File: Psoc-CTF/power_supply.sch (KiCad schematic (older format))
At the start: 12 parts

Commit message: Generación de lista de materiales
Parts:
- gave numbers to parts that had none: 12
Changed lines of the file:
@@
 $EndDescr
 $Comp
-L Regulator_Linear:AMS1117-5.0 U?
+L Regulator_Linear:AMS1117-5.0 U2
 U 1 1 621012EE
 P 2050 1700
-F 0 "U?" H 2050 1942 50  0000 C CNN
+F 0 "U2" H 2050 1942 50  0000 C CNN
 F 1 "AMS1117-5.0" H 2050 1851 50  0000 C CNN
 F 2 "Package_TO_SOT_SMD:SOT-223-3_TabPin2" H 2050 1900 50  0001 C CNN
@@
 $EndComp
 $Comp
-L Device:C C?
+L Device:C C5
 U 1 1 621012F4
 P 2950 1850
-F 0 "C?" H 3065 1896 50  0000 L CNN
+F 0 "C5" H 3065 1896 50  0000 L CNN
 F 1 "10uF" H 3065 1805 50  0000 L CNN
 F 2 "Capacitor_SMD:C_0603_1608Metric_Pad1.08x0.95mm_HandSolder" H 2988 1700 50  0001 C CNN
@@
 $EndComp
 $Comp
-L Device:CP C?
+L Device:CP C1
 U 1 1 621012FA
 P 1450 1850
-F 0 "C?" H 1568 1896 50  0000 L CNN
+F 0 "C1" H 1568 1896 50  0000 L CNN
 F 1 "100uF" H 1568 1805 50  0000 L CNN
 F 2 "Capacitor_SMD:C_0805_2012Metric_Pad1.18x1.45mm_HandSolder" H 1488 1700 50  0001 C CNN
@@
 $EndComp
 $Comp
-L Device:CP C?
+L Device:CP C3
 U 1 1 62101300
 P 2500 1850
-F 0 "C?" H 2618 1896 50  0000 L CNN
+F 0 "C3" H 2618 1896 50  0000 L CNN
 F 1 "10uF" H 2618 1805 50  0000 L CNN
 F 2 "Capacitor_SMD:C_0805_2012Metric_Pad1.18x1.45mm_HandSolder" H 2538 1700 50  0001 C CNN
@@
 Vin
 $Comp
-L power:GND #PWR?
+L power:GND #PWR05
 U 1 1 62101312
 P 2050 2000
-F 0 "#PWR?" H 2050 1750 50  0001 C CNN
+F 0 "#PWR05" H 2050 1750 50  0001 C CNN
 F 1 "GND" H 2055 1827 50  0000 C CNN
 F 2 "" H 2050 2000 50  0001 C CNN
@@
 Connection ~ 1800 3375
 $Comp
-L power:GND #PWR?
+L power:GND #PWR04
 U 1 1 62101319
 P 1800 3375
-F 0 "#PWR?" H 1800 3125 50  0001 C CNN
+F 0 "#PWR04" H 1800 3125 50  0001 C CNN
 F 1 "GND" H 1805 3202 50  0000 C CNN
 F 2 "" H 1800 3375 50  0001 C CNN
@@
 	2100 3075 2300 3075
 $Comp
-L Device:C C?
+L Device:C C4
 U 1 1 62101325
 P 2750 3225
-F 0 "C?" H 2865 3271 50  0000 L CNN
+F 0 "C4" H 2865 3271 50  0000 L CNN
 F 1 "10uF" H 2865 3180 50  0000 L CNN
 F 2 "Capacitor_SMD:C_0603_1608Metric_Pad1.08x0.95mm_HandSolder" H 2788 3075 50  0001 C CNN
@@
 $EndComp
 $Comp
-L Device:CP C?
+L Device:CP C2
 U 1 1 6210132B
 P 2300 3225
-F 0 "C?" H 2418 3271 50  0000 L CNN
+F 0 "C2" H 2418 3271 50  0000 L CNN
 F 1 "10uF" H 2418 3180 50  0000 L CNN
 F 2 "Capacitor_SMD:C_0805_2012Metric_Pad1.18x1.45mm_HandSolder" H 2338 3075 50  0001 C CNN
@@
 	1250 3075 1500 3075
 $Comp
-L Regulator_Linear:AMS1117-3.3 U?
+L Regulator_Linear:AMS1117-3.3 U1
 U 1 1 62101332
 P 1800 3075
-F 0 "U?" H 1800 3317 50  0000 C CNN
+F 0 "U1" H 1800 3317 50  0000 C CNN
 F 1 "AMS1117-3.3" H 1800 3226 50  0000 C CNN
 F 2 "Package_TO_SOT_SMD:SOT-223-3_TabPin2" H 1800 3275 50  0001 C CNN
@@
 3.3V POWER SUPPLY
 $Comp
-L power:+3.3V #PWR?
+L power:+3.3V #PWR09
 U 1 1 6210133B
 P 2750 3075
-F 0 "#PWR?" H 2750 2925 50  0001 C CNN
+F 0 "#PWR09" H 2750 2925 50  0001 C CNN
 F 1 "+3.3V" H 2765 3248 50  0000 C CNN
 F 2 "" H 2750 3075 50  0001 C CNN
@@
 Connection ~ 2750 3075
 $Comp
-L power:+5V #PWR?
+L power:+5V #PWR02
 U 1 1 62101342
 P 1250 3075
-F 0 "#PWR?" H 1250 2925 50  0001 C CNN
+F 0 "#PWR02" H 1250 2925 50  0001 C CNN
 F 1 "+5V" H 1250 3250 50  0000 C CNN
 F 2 "" H 1250 3075 50  0001 C CNN
@@
 P 1600 4050
 AR Path="/621106AB" Ref="#PWR?"  Part="1"
-AR Path="/620E3406/621106AB" Ref="#PWR?"  Part="1"
-F 0 "#PWR?" H 1600 3900 50  0001 C CNN
+AR Path="/620E3406/621106AB" Ref="#PWR03"  Part="1"
+F 0 "#PWR03" H 1600 3900 50  0001 C CNN
 F 1 "VDD" V 1600 4175 50  0000 L CNN
 F 2 "" H 1600 4050 50  0001 C CNN
@@
 P 1100 4050
 AR Path="/621106B4" Ref="#PWR?"  Part="1"
-AR Path="/620E3406/621106B4" Ref="#PWR?"  Part="1"
-F 0 "#PWR?" H 1100 3900 50  0001 C CNN
+AR Path="/620E3406/621106B4" Ref="#PWR01"  Part="1"
+F 0 "#PWR01" H 1100 3900 50  0001 C CNN
 F 1 "+3.3V" V 1100 4325 50  0000 C CNN
 F 2 "" H 1100 4050 50  0001 C CNN
@@
 P 2500 4225
 AR Path="/621106C5" Ref="#PWR?"  Part="1"
-AR Path="/620E3406/621106C5" Ref="#PWR?"  Part="1"
-F 0 "#PWR?" H 2500 4075 50  0001 C CNN
+AR Path="/620E3406/621106C5" Ref="#PWR08"  Part="1"
+F 0 "#PWR08" H 2500 4075 50  0001 C CNN
 F 1 "+5V" V 2475 4400 50  0000 C CNN
 F 2 "" H 2500 4225 50  0001 C CNN
@@
 P 2300 4225
 AR Path="/621106CB" Ref="J?"  Part="1"
-AR Path="/620E3406/621106CB" Ref="J?"  Part="1"
-F 0 "J?" H 2218 4542 50  0000 C CNN
+AR Path="/620E3406/621106CB" Ref="J1"  Part="1"
+F 0 "J1" H 2218 4542 50  0000 C CNN
 F 1 "Conn_01x03" H 2218 4451 50  0000 C CNN
 F 2 "" H 2300 4225 50  0001 C CNN
@@
 P 2200 5850
 AR Path="/6211D42D" Ref="D?"  Part="1"
-AR Path="/620E3406/6211D42D" Ref="D?"  Part="1"
-F 0 "D?" V 2193 6067 50  0000 C CNN
+AR Path="/620E3406/6211D42D" Ref="D2"  Part="1"
+F 0 "D2" V 2193 6067 50  0000 C CNN
 F 1 "LED" V 2100 6050 50  0000 C CNN
 F 2 "" H 2200 5850 50  0001 C CNN
@@
 P 2200 5550
 AR Path="/6211D433" Ref="R?"  Part="1"
-AR Path="/620E3406/6211D433" Ref="R?"  Part="1"
-F 0 "R?" H 1993 5550 50  0000 C CNN
+AR Path="/620E3406/6211D433" Ref="R1"  Part="1"
+F 0 "R1" H 1993 5550 50  0000 C CNN
 F 1 "1K" H 2000 5450 50  0000 C CNN
 F 2 "Resistor_SMD:R_0603_1608Metric_Pad0.98x0.95mm_HandSolder" V 2130 5550 50  0001 C CNN
@@
 P 2200 5400
 AR Path="/6211D439" Ref="#PWR?"  Part="1"
-AR Path="/620E3406/6211D439" Ref="#PWR?"  Part="1"
-F 0 "#PWR?" H 2200 5250 50  0001 C CNN
+AR Path="/620E3406/6211D439" Ref="#PWR06"  Part="1"
+F 0 "#PWR06" H 2200 5250 50  0001 C CNN
 F 1 "VDD" H 2100 5550 50  0000 L CNN
 F 2 "" H 2200 5400 50  0001 C CNN
@@
 P 2200 6000
 AR Path="/6211D43F" Ref="#PWR?"  Part="1"
-AR Path="/620E3406/6211D43F" Ref="#PWR?"  Part="1"
-F 0 "#PWR?" H 2200 5750 50  0001 C CNN
+AR Path="/620E3406/6211D43F" Ref="#PWR07"  Part="1"
+F 0 "#PWR07" H 2200 5750 50  0001 C CNN
 F 1 "GND" H 2200 5850 50  0000 R CNN
 F 2 "" H 2200 6000 50  0001 C CNN
@@
 P 4400 1950
 AR Path="/621350E1" Ref="#PWR?"  Part="1"
-AR Path="/620E3406/621350E1" Ref="#PWR?"  Part="1"
-F 0 "#PWR?" H 4400 1700 50  0001 C CNN
+AR Path="/620E3406/621350E1" Ref="#PWR010"  Part="1"
+F 0 "#PWR010" H 4400 1700 50  0001 C CNN
 F 1 "GND" H 4475 1775 50  0000 R CNN
 F 2 "" H 4400 1950 50  0001 C CNN
@@
 P 4125 1900
 AR Path="/621350E7" Ref="J?"  Part="1"
-AR Path="/620E3406/621350E7" Ref="J?"  Part="1"
-F 0 "J?" H 4043 1575 50  0000 C CNN
+AR Path="/620E3406/621350E7" Ref="J2"  Part="1"
+F 0 "J2" H 4043 1575 50  0000 C CNN
 F 1 "Conn_01x02" H 4043 1666 50  0000 C CNN
 F 2 "" H 4125 1900 50  0001 C CNN
@@
 5VSERIAL
 $Comp
-L pspice:DIODE D?
+L pspice:DIODE D1
 U 1 1 621D0263
 P 1350 4050
-F 0 "D?" H 1350 4315 50  0000 C CNN
+F 0 "D1" H 1350 4315 50  0000 C CNN
 F 1 "DIODE" H 1350 4224 50  0000 C CNN
 F 2 "" H 1350 4050 50  0001 C CNN

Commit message: Archivo Cache para cadlab
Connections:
- net labels added: +12V
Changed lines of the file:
@@
 $EndComp
-Wire Wire Line
-	1450 1700 1750 1700
 Wire Wire Line
 	1450 2000 2050 2000
@@
 Wire Wire Line
 	1450 1700 1150 1700
-Connection ~ 1450 1700
-Text Label 1150 1700 0    50   ~ 0
-Vin
 $Comp
 L power:GND #PWR05
@@
 Wire Wire Line
 	1550 4050 1600 4050
+Text HLabel 1150 1700 0    50   Input ~ 0
+Vin
+Wire Wire Line
+	1450 1700 1750 1700
+Connection ~ 1450 1700
+$Comp
+L power:+12V #PWR0101
+U 1 1 62124F62
+P 1450 1700
+F 0 "#PWR0101" H 1450 1550 50  0001 C CNN
+F 1 "+12V" H 1465 1873 50  0000 C CNN
+F 2 "" H 1450 1700 50  0001 C CNN
+F 3 "" H 1450 1700 50  0001 C CNN
+	1    1450 1700
+	1    0    0    -1
+$EndComp
 $EndSCHEMATC

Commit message: Se retira las memorias flash y Ram por spi y se coloca una F-RAM por i2c
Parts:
- added R1: 0, Resistor_SMD:R_0805_2012Metric_Pad1.20x1.40mm_HandSolder, symbol Device:R
- D1: value DIODE -> EGF1D; footprint (none) -> Diode_SMD:D_SMA_Handsoldering
- D2: footprint (none) -> LED_SMD:LED_0603_1608Metric_Pad1.05x0.95mm_HandSolder
- J1: footprint (none) -> Connector_PinHeader_2.54mm:PinHeader_1x03_P2.54mm_Vertical
- J2: footprint (none) -> Connector_PinHeader_2.54mm:PinHeader_1x02_P2.54mm_Vertical
- renumbered R1 to R2
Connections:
- wire segments 19 -> 25
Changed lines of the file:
@@
 	1450 1700 1150 1700
 $Comp
-L power:GND #PWR05
+L power:GND #PWR06
 U 1 1 62101312
 P 2050 2000
-F 0 "#PWR05" H 2050 1750 50  0001 C CNN
+F 0 "#PWR06" H 2050 1750 50  0001 C CNN
 F 1 "GND" H 2055 1827 50  0000 C CNN
 F 2 "" H 2050 2000 50  0001 C CNN
@@
 Connection ~ 1800 3375
 $Comp
-L power:GND #PWR04
+L power:GND #PWR05
 U 1 1 62101319
 P 1800 3375
-F 0 "#PWR04" H 1800 3125 50  0001 C CNN
+F 0 "#PWR05" H 1800 3125 50  0001 C CNN
 F 1 "GND" H 1805 3202 50  0000 C CNN
 F 2 "" H 1800 3375 50  0001 C CNN
@@
 3.3V POWER SUPPLY
 $Comp
-L power:+3.3V #PWR09
+L power:+3.3V #PWR010
 U 1 1 6210133B
 P 2750 3075
-F 0 "#PWR09" H 2750 2925 50  0001 C CNN
+F 0 "#PWR010" H 2750 2925 50  0001 C CNN
 F 1 "+3.3V" H 2765 3248 50  0000 C CNN
 F 2 "" H 2750 3075 50  0001 C CNN
@@
 L power:VDD #PWR?
 U 1 1 621106AB
-P 1600 4050
+P 1775 4050
 AR Path="/621106AB" Ref="#PWR?"  Part="1"
-AR Path="/620E3406/621106AB" Ref="#PWR03"  Part="1"
-F 0 "#PWR03" H 1600 3900 50  0001 C CNN
-F 1 "VDD" V 1600 4175 50  0000 L CNN
-F 2 "" H 1600 4050 50  0001 C CNN
-F 3 "" H 1600 4050 50  0001 C CNN
-	1    1600 4050
+AR Path="/620E3406/621106AB" Ref="#PWR04"  Part="1"
+F 0 "#PWR04" H 1775 3900 50  0001 C CNN
+F 1 "VDD" V 1775 4175 50  0000 L CNN
+F 2 "" H 1775 4050 50  0001 C CNN
+F 3 "" H 1775 4050 50  0001 C CNN
+	1    1775 4050
 	0    1    1    0
 $EndComp
@@
 L power:+3.3V #PWR?
 U 1 1 621106B4
-P 1100 4050
+P 875 4050
 AR Path="/621106B4" Ref="#PWR?"  Part="1"
 AR Path="/620E3406/621106B4" Ref="#PWR01"  Part="1"
-F 0 "#PWR01" H 1100 3900 50  0001 C CNN
-F 1 "+3.3V" V 1100 4325 50  0000 C CNN
-F 2 "" H 1100 4050 50  0001 C CNN
-F 3 "" H 1100 4050 50  0001 C CNN
-	1    1100 4050
+F 0 "#PWR01" H 875 3900 50  0001 C CNN
+F 1 "+3.3V" V 875 4325 50  0000 C CNN
+F 2 "" H 875 4050 50  0001 C CNN
+F 3 "" H 875 4050 50  0001 C CNN
+	1    875  4050
 	0    -1   -1   0
 $EndComp
@@
 P 2500 4225
 AR Path="/621106C5" Ref="#PWR?"  Part="1"
-AR Path="/620E3406/621106C5" Ref="#PWR08"  Part="1"
-F 0 "#PWR08" H 2500 4075 50  0001 C CNN
+AR Path="/620E3406/621106C5" Ref="#PWR09"  Part="1"
+F 0 "#PWR09" H 2500 4075 50  0001 C CNN
 F 1 "+5V" V 2475 4400 50  0000 C CNN
 F 2 "" H 2500 4225 50  0001 C CNN
@@
 F 0 "J1" H 2218 4542 50  0000 C CNN
 F 1 "Conn_01x03" H 2218 4451 50  0000 C CNN
-F 2 "" H 2300 4225 50  0001 C CNN
+F 2 "Connector_PinHeader_2.54mm:PinHeader_1x03_P2.54mm_Vertical" H 2300 4225 50  0001 C CNN
 F 3 "~" H 2300 4225 50  0001 C CNN
 	1    2300 4225
@@
 F 0 "D2" V 2193 6067 50  0000 C CNN
 F 1 "LED" V 2100 6050 50  0000 C CNN
-F 2 "" H 2200 5850 50  0001 C CNN
+F 2 "LED_SMD:LED_0603_1608Metric_Pad1.05x0.95mm_HandSolder" H 2200 5850 50  0001 C CNN
 F 3 "~" H 2200 5850 50  0001 C CNN
 	1    2200 5850
@@
 P 2200 5550
 AR Path="/6211D433" Ref="R?"  Part="1"
-AR Path="/620E3406/6211D433" Ref="R1"  Part="1"
-F 0 "R1" H 1993 5550 50  0000 C CNN
+AR Path="/620E3406/6211D433" Ref="R2"  Part="1"
+F 0 "R2" H 1993 5550 50  0000 C CNN
 F 1 "1K" H 2000 5450 50  0000 C CNN
 F 2 "Resistor_SMD:R_0603_1608Metric_Pad0.98x0.95mm_HandSolder" V 2130 5550 50  0001 C CNN
@@
 P 2200 5400
 AR Path="/6211D439" Ref="#PWR?"  Part="1"
-AR Path="/620E3406/6211D439" Ref="#PWR06"  Part="1"
-F 0 "#PWR06" H 2200 5250 50  0001 C CNN
+AR Path="/620E3406/6211D439" Ref="#PWR07"  Part="1"
+F 0 "#PWR07" H 2200 5250 50  0001 C CNN
 F 1 "VDD" H 2100 5550 50  0000 L CNN
 F 2 "" H 2200 5400 50  0001 C CNN
@@
 P 2200 6000
 AR Path="/6211D43F" Ref="#PWR?"  Part="1"
-AR Path="/620E3406/6211D43F" Ref="#PWR07"  Part="1"
-F 0 "#PWR07" H 2200 5750 50  0001 C CNN
+AR Path="/620E3406/6211D43F" Ref="#PWR08"  Part="1"
+F 0 "#PWR08" H 2200 5750 50  0001 C CNN
 F 1 "GND" H 2200 5850 50  0000 R CNN
 F 2 "" H 2200 6000 50  0001 C CNN
@@
 P 4400 1950
 AR Path="/621350E1" Ref="#PWR?"  Part="1"
-AR Path="/620E3406/621350E1" Ref="#PWR010"  Part="1"
-F 0 "#PWR010" H 4400 1700 50  0001 C CNN
+AR Path="/620E3406/621350E1" Ref="#PWR011"  Part="1"
+F 0 "#PWR011" H 4400 1700 50  0001 C CNN
 F 1 "GND" H 4475 1775 50  0000 R CNN
 F 2 "" H 4400 1950 50  0001 C CNN
@@
 F 0 "J2" H 4043 1575 50  0000 C CNN
 F 1 "Conn_01x02" H 4043 1666 50  0000 C CNN
-F 2 "" H 4125 1900 50  0001 C CNN
+F 2 "Connector_PinHeader_2.54mm:PinHeader_1x02_P2.54mm_Vertical" H 4125 1900 50  0001 C CNN
 F 3 "~" H 4125 1900 50  0001 C CNN
 	1    4125 1900
@@
 P 1350 4050
 F 0 "D1" H 1350 4315 50  0000 C CNN
-F 1 "DIODE" H 1350 4224 50  0000 C CNN
-F 2 "" H 1350 4050 50  0001 C CNN
-F 3 "~" H 1350 4050 50  0001 C CNN
+F 1 "EGF1D" H 1350 4224 50  0000 C CNN
+F 2 "Diode_SMD:D_SMA_Handsoldering" H 1350 4050 50  0001 C CNN
+F 3 "https://rocelec.widen.net/view/pdf/pkddtwhpuh/ONSM-S-A0003590693-1.pdf?t.download=true&u=5oefqw" H 1350 4050 50  0001 C CNN
 	1    1350 4050
 	1    0    0    -1
@@
 	1150 4050 1100 4050
 Wire Wire Line
-	1550 4050 1600 4050
+	1550 4050 1625 4050
 Text HLabel 1150 1700 0    50   Input ~ 0
 Vin
-Wire Wire Line
-	1450 1700 1750 1700
 Connection ~ 1450 1700
 $Comp
-L power:+12V #PWR0101
+L power:+12V #PWR03
 U 1 1 62124F62
 P 1450 1700
-F 0 "#PWR0101" H 1450 1550 50  0001 C CNN
+F 0 "#PWR03" H 1450 1550 50  0001 C CNN
 F 1 "+12V" H 1465 1873 50  0000 C CNN
 F 2 "" H 1450 1700 50  0001 C CNN
@@
 	1    0    0    -1
 $EndComp
+Wire Wire Line
+	1750 1700 1450 1700
+$Comp
+L Device:R R?
+U 1 1 6226B9FA
+P 1325 4325
+AR Path="/6226B9FA" Ref="R?"  Part="1"
+AR Path="/620E3406/6226B9FA" Ref="R1"  Part="1"
+F 0 "R1" V 1425 4325 50  0000 C CNN
+F 1 "0" V 1500 4325 50  0000 C CNN
+F 2 "Resistor_SMD:R_0805_2012Metric_Pad1.20x1.40mm_HandSolder" V 1255 4325 50  0001 C CNN
+F 3 "~" H 1325 4325 50  0001 C CNN
+	1    1325 4325
+	0    1    1    0
+$EndComp
+Wire Wire Line
+	1175 4325 1100 4325
+Wire Wire Line
+	1100 4325 1100 4050
+Connection ~ 1100 4050
+Wire Wire Line
+	1100 4050 875  4050
+Wire Wire Line
+	1475 4325 1625 4325
+Wire Wire Line
+	1625 4325 1625 4050
+Connection ~ 1625 4050
+Wire Wire Line
+	1625 4050 1775 4050
 $EndSCHEMATC

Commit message: Antena agregada, pines de programación SWD
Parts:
- added D1: SSA14, Diode_SMD:D_SMA_Handsoldering, symbol Device:D_Schottky
- D2: renamed from D1; value EGF1D -> SSA14; symbol pspice:DIODE -> Device:D_Schottky
- renumbered C3 to C2, C2 to C3, C5 to C4, C4 to C5, D2 to D3, J2 to J1, J1 to J2, U2 to U1, U1 to U2
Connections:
- net labels added: 3V3SWD, 5VBUS
- net labels removed: 5VSERIAL
- wire segments 25 -> 28
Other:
- note added: "AMMETER JUMPER"
- moved on the sheet: C1, C2, C4, J2, R1, U1, U2

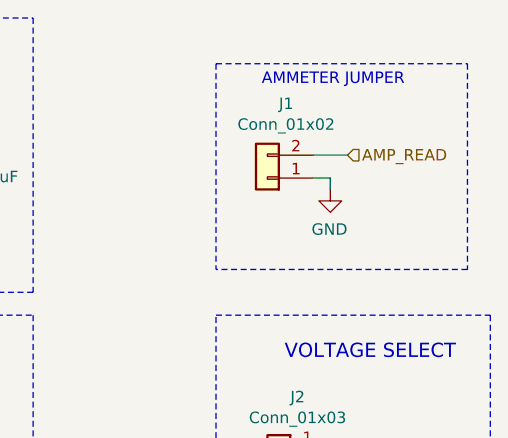
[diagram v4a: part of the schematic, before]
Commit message: Anexo de nuevos pulsadores y arreglo de resistencias
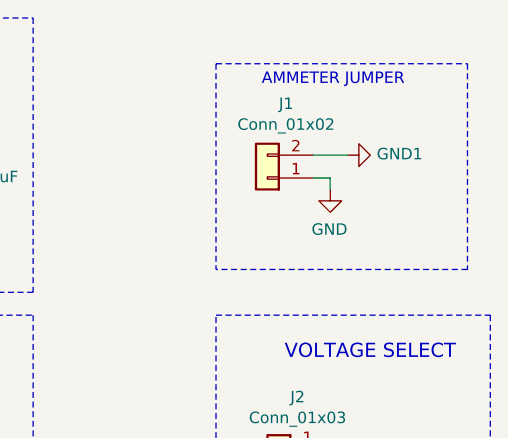
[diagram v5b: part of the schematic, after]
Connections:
- net AMP_READ renamed GND1
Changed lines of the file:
@@
 	-1   0    0    1
 $EndComp
-Text HLabel 4475 1800 2    50   Input ~ 0
-AMP_READ
 $Comp
 L Device:D_Schottky D2
@@
 Wire Wire Line
 	4400 1900 4400 1950
+$Comp
+L power:GND1 #PWR056
+U 1 1 622A7FA3
+P 4475 1800
+F 0 "#PWR056" H 4475 1550 50  0001 C CNN
+F 1 "GND1" V 4480 1672 50  0000 R CNN
+F 2 "" H 4475 1800 50  0001 C CNN
+F 3 "" H 4475 1800 50  0001 C CNN
+	1    4475 1800
+	0    -1   -1   0
+$EndComp
 $EndSCHEMATC

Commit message: Ruteo Psoc-CTF
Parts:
- added C40: 10uF, Capacitor_SMD:C_0805_2012Metric_Pad1.18x1.45mm_HandSolder, symbol Device:CP
- added C41: 10uF, Capacitor_SMD:C_0603_1608Metric_Pad1.08x0.95mm_HandSolder, symbol Device:C
- added U6: AMS1117-3.3, Package_TO_SOT_SMD:SOT-223-3_TabPin2, symbol Regulator_Linear:AMS1117-3.3
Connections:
- net +3V3: now also C40.1, C41.1, U6.2 (VO)
- net +5V: now also U6.3 (VI)
- net GND: now also C40.2, C41.2, U6.1 (GND)
- net 5VBUS renamed VBUS
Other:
- note added: "ESP POWER SUPPLY"
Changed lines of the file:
@@
 	2300 1700 2750 1700
 Connection ~ 2300 1700
-Wire Wire Line
-	1250 1700 950  1700
 $Comp
 L power:GND #PWR04
@@
 Wire Wire Line
 	2300 4075 2425 4075
-Text HLabel 950  1700 0    50   Input ~ 0
-Vin
 Connection ~ 1250 1700
 $Comp
@@
 3V3SWD
 Text HLabel 4700 3075 2    50   Input ~ 0
-5VBUS
+VBUS
 Wire Wire Line
 	1875 3850 1900 3850
@@
 	0    -1   -1   0
 $EndComp
+$Comp
+L power:+3V3 #PWR014
+U 1 1 62395ED8
+P 5075 4575
+F 0 "#PWR014" H 5075 4425 50  0001 C CNN
+F 1 "+3V3" H 5090 4748 50  0000 C CNN
+F 2 "" H 5075 4575 50  0001 C CNN
+F 3 "" H 5075 4575 50  0001 C CNN
+	1    5075 4575
+	1    0    0    -1
+$EndComp
+Connection ~ 4250 4875
+$Comp
+L power:GND #PWR013
+U 1 1 6239862F
+P 4250 4875
+F 0 "#PWR013" H 4250 4625 50  0001 C CNN
+F 1 "GND" H 4255 4702 50  0000 C CNN
+F 2 "" H 4250 4875 50  0001 C CNN
+F 3 "" H 4250 4875 50  0001 C CNN
+	1    4250 4875
+	1    0    0    -1
+$EndComp
+Connection ~ 4625 4875
+Wire Wire Line
+	4625 4875 5075 4875
+Wire Wire Line
+	4250 4875 4625 4875
+Connection ~ 4625 4575
+Wire Wire Line
+	4625 4575 5075 4575
+Wire Wire Line
+	4550 4575 4625 4575
+$Comp
+L Device:C C41
+U 1 1 6239863B
+P 5075 4725
+F 0 "C41" H 5190 4771 50  0000 L CNN
+F 1 "10uF" H 5190 4680 50  0000 L CNN
+F 2 "Capacitor_SMD:C_0603_1608Metric_Pad1.08x0.95mm_HandSolder" H 5113 4575 50  0001 C CNN
+F 3 "~" H 5075 4725 50  0001 C CNN
+	1    5075 4725
+	1    0    0    -1
+$EndComp
+$Comp
+L Device:CP C40
+U 1 1 62398641
+P 4625 4725
+F 0 "C40" H 4743 4771 50  0000 L CNN
+F 1 "10uF" H 4743 4680 50  0000 L CNN
+F 2 "Capacitor_SMD:C_0805_2012Metric_Pad1.18x1.45mm_HandSolder" H 4663 4575 50  0001 C CNN
+F 3 "~" H 4625 4725 50  0001 C CNN
+	1    4625 4725
+	1    0    0    -1
+$EndComp
+Wire Wire Line
+	3800 4575 3950 4575
+$Comp
+L Regulator_Linear:AMS1117-3.3 U6
+U 1 1 62398648
+P 4250 4575
+F 0 "U6" H 4250 4817 50  0000 C CNN
+F 1 "AMS1117-3.3" H 4250 4726 50  0000 C CNN
+F 2 "Package_TO_SOT_SMD:SOT-223-3_TabPin2" H 4250 4775 50  0001 C CNN
+F 3 "http://www.advanced-monolithic.com/pdf/ds1117.pdf" H 4350 4325 50  0001 C CNN
+	1    4250 4575
+	1    0    0    -1
+$EndComp
+Text Notes 3900 4200 0    62   ~ 0
+ESP POWER SUPPLY
+$Comp
+L power:+5V #PWR012
+U 1 1 62398656
+P 3800 4575
+F 0 "#PWR012" H 3800 4425 50  0001 C CNN
+F 1 "+5V" H 3800 4750 50  0000 C CNN
+F 2 "" H 3800 4575 50  0001 C CNN
+F 3 "" H 3800 4575 50  0001 C CNN
+	1    3800 4575
+	1    0    0    -1
+$EndComp
+Connection ~ 5075 4575
 $EndSCHEMATC
